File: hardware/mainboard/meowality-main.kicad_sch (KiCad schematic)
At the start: 0 parts

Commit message: Initial 'floorplan' outline
Signed-off-by: gatecat <gatecat@ds0.me>
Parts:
- added H? (x10): MountingHole_Pad, MountingHole:MountingHole_2.7mm_M2.5_Pad_Via, symbol Mechanical:MountingHole_Pad
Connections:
- new net GND: H?.1, H?.1, H?.1, H?.1, H?.1, H?.1, H?.1, H?.1, H?.1, H?.1

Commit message: Placement snapshot
Signed-off-by: gatecat <gatecat@ds0.me>
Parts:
- gave numbers to parts that had none: 10
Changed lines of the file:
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@@
   (symbol (lib_id "power:GND") (at 198.12 97.79 0) (unit 1)
     (in_bom yes) (on_board yes) (fields_autoplaced)
-    (property "Reference" "#PWR?" (id 0) (at 198.12 104.14 0)
+    (property "Reference" "#PWR0300" (id 0) (at 198.12 104.14 0)
       (effects (font (size 1.27 1.27)) hide)
     )
@@
   (symbol (lib_id "Mechanical:MountingHole_Pad") (at 152.4 90.17 0) (unit 1)
     (in_bom yes) (on_board yes) (fields_autoplaced)
-    (property "Reference" "H?" (id 0) (at 154.94 87.6299 0)
+    (property "Reference" "H1" (id 0) (at 154.94 87.6299 0)
       (effects (font (size 1.27 1.27)) (justify left) hide)
     )
@@
   (symbol (lib_id "Mechanical:MountingHole_Pad") (at 193.04 90.17 0) (unit 1)
     (in_bom yes) (on_board yes) (fields_autoplaced)
-    (property "Reference" "H?" (id 0) (at 195.58 87.6299 0)
+    (property "Reference" "H9" (id 0) (at 195.58 87.6299 0)
       (effects (font (size 1.27 1.27)) (justify left) hide)
     )
@@
   (symbol (lib_id "Mechanical:MountingHole_Pad") (at 162.56 90.17 0) (unit 1)
     (in_bom yes) (on_board yes) (fields_autoplaced)
-    (property "Reference" "H?" (id 0) (at 165.1 87.6299 0)
+    (property "Reference" "H3" (id 0) (at 165.1 87.6299 0)
       (effects (font (size 1.27 1.27)) (justify left) hide)
     )
@@
   (symbol (lib_id "Mechanical:MountingHole_Pad") (at 172.72 90.17 0) (unit 1)
     (in_bom yes) (on_board yes) (fields_autoplaced)
-    (property "Reference" "H?" (id 0) (at 175.26 87.6299 0)
+    (property "Reference" "H5" (id 0) (at 175.26 87.6299 0)
       (effects (font (size 1.27 1.27)) (justify left) hide)
     )
@@
   (symbol (lib_id "Mechanical:MountingHole_Pad") (at 157.48 90.17 0) (unit 1)
     (in_bom yes) (on_board yes) (fields_autoplaced)
-    (property "Reference" "H?" (id 0) (at 160.02 87.6299 0)
+    (property "Reference" "H2" (id 0) (at 160.02 87.6299 0)
       (effects (font (size 1.27 1.27)) (justify left) hide)
     )
@@
   (symbol (lib_id "Mechanical:MountingHole_Pad") (at 177.8 90.17 0) (unit 1)
     (in_bom yes) (on_board yes) (fields_autoplaced)
-    (property "Reference" "H?" (id 0) (at 180.34 87.6299 0)
+    (property "Reference" "H6" (id 0) (at 180.34 87.6299 0)
       (effects (font (size 1.27 1.27)) (justify left) hide)
     )
@@
   (symbol (lib_id "Mechanical:MountingHole_Pad") (at 198.12 90.17 0) (unit 1)
     (in_bom yes) (on_board yes) (fields_autoplaced)
-    (property "Reference" "H?" (id 0) (at 200.66 87.6299 0)
+    (property "Reference" "H10" (id 0) (at 200.66 87.6299 0)
       (effects (font (size 1.27 1.27)) (justify left) hide)
     )
@@
   (symbol (lib_id "Mechanical:MountingHole_Pad") (at 187.96 90.17 0) (unit 1)
     (in_bom yes) (on_board yes) (fields_autoplaced)
-    (property "Reference" "H?" (id 0) (at 190.5 87.6299 0)
+    (property "Reference" "H8" (id 0) (at 190.5 87.6299 0)
       (effects (font (size 1.27 1.27)) (justify left) hide)
     )
@@
   (symbol (lib_id "Mechanical:MountingHole_Pad") (at 167.64 90.17 0) (unit 1)
     (in_bom yes) (on_board yes) (fields_autoplaced)
-    (property "Reference" "H?" (id 0) (at 170.18 87.6299 0)
+    (property "Reference" "H4" (id 0) (at 170.18 87.6299 0)
       (effects (font (size 1.27 1.27)) (justify left) hide)
     )
@@
   (symbol (lib_id "Mechanical:MountingHole_Pad") (at 182.88 90.17 0) (unit 1)
     (in_bom yes) (on_board yes) (fields_autoplaced)
-    (property "Reference" "H?" (id 0) (at 185.42 87.6299 0)
+    (property "Reference" "H7" (id 0) (at 185.42 87.6299 0)
       (effects (font (size 1.27 1.27)) (justify left) hide)
     )
@@
       (reference "#PWR0299") (unit 1) (value "+3V3PL") (footprint "")
     )
+    (path "/29964473-8088-4ef2-86ea-4668a18d61fb"
+      (reference "#PWR0300") (unit 1) (value "GND") (footprint "")
+    )
     (path "/1fd619f4-b635-4feb-bd8e-d44522069ea8/6d520754-68d8-4942-8352-d8883ee61a70"
       (reference "#PWR0303") (unit 1) (value "GND") (footprint "")
@@
       (reference "#PWR0367") (unit 1) (value "+3V3PS") (footprint "")
     )
-    (path "/29964473-8088-4ef2-86ea-4668a18d61fb"
-      (reference "#PWR?") (unit 1) (value "GND") (footprint "")
-    )
     (path "/a559f63f-b3a0-4b81-aa6a-605d4da47af6/ec041bff-8a9c-4cb6-b71e-875f2b8c18d1"
       (reference "C1") (unit 1) (value "10µ") (footprint "Capacitor_SMD:C_1206_3216Metric")
@@
     )
     (path "/84ae9301-5488-428b-9d51-06c46b2f0897"
-      (reference "H?") (unit 1) (value "MountingHole_Pad") (footprint "MountingHole:MountingHole_2.7mm_M2.5_Pad_Via")
+      (reference "H1") (unit 1) (value "MountingHole_Pad") (footprint "MountingHole:MountingHole_2.7mm_M2.5_Pad_Via")
+    )
+    (path "/a9b15bc8-d58f-4dce-8008-aeed89e9068b"
+      (reference "H2") (unit 1) (value "MountingHole_Pad") (footprint "MountingHole:MountingHole_2.7mm_M2.5_Pad_Via")
+    )
+    (path "/a070b648-0a85-4170-8a91-599450342e60"
+      (reference "H3") (unit 1) (value "MountingHole_Pad") (footprint "MountingHole:MountingHole_2.7mm_M2.5_Pad_Via")
+    )
+    (path "/e83ea659-2f37-4a3f-a914-2fd0ea472ff3"
+      (reference "H4") (unit 1) (value "MountingHole_Pad") (footprint "MountingHole:MountingHole_2.7mm_M2.5_Pad_Via")
+    )
+    (path "/a34472c6-e5af-4466-bd8c-00051220b9a1"
+      (reference "H5") (unit 1) (value "MountingHole_Pad") (footprint "MountingHole:MountingHole_2.7mm_M2.5_Pad_Via")
+    )
+    (path "/ba6ddcc1-2647-425e-ab4b-d4ffcf66f14b"
+      (reference "H6") (unit 1) (value "MountingHole_Pad") (footprint "MountingHole:MountingHole_2.7mm_M2.5_Pad_Via")
+    )
+    (path "/fc07208b-6f96-45bd-97dc-c33438e49527"
+      (reference "H7") (unit 1) (value "MountingHole_Pad") (footprint "MountingHole:MountingHole_2.7mm_M2.5_Pad_Via")
+    )
+    (path "/e57d0bad-e8df-4b6c-aa3e-bc3f8fd9b788"
+      (reference "H8") (unit 1) (value "MountingHole_Pad") (footprint "MountingHole:MountingHole_2.7mm_M2.5_Pad_Via")
     )
     (path "/9a9fcb89-1441-4dc8-8161-d4c2ca88b33e"
-      (reference "H?") (unit 1) (value "MountingHole_Pad") (footprint "MountingHole:MountingHole_2.7mm_M2.5_Pad_Via")
-    )
-    (path "/a070b648-0a85-4170-8a91-599450342e60"
-      (reference "H?") (unit 1) (value "MountingHole_Pad") (footprint "MountingHole:MountingHole_2.7mm_M2.5_Pad_Via")
-    )
-    (path "/a34472c6-e5af-4466-bd8c-00051220b9a1"
-      (reference "H?") (unit 1) (value "MountingHole_Pad") (footprint "MountingHole:MountingHole_2.7mm_M2.5_Pad_Via")
-    )
-    (path "/a9b15bc8-d58f-4dce-8008-aeed89e9068b"
-      (reference "H?") (unit 1) (value "MountingHole_Pad") (footprint "MountingHole:MountingHole_2.7mm_M2.5_Pad_Via")
-    )
-    (path "/ba6ddcc1-2647-425e-ab4b-d4ffcf66f14b"
-      (reference "H?") (unit 1) (value "MountingHole_Pad") (footprint "MountingHole:MountingHole_2.7mm_M2.5_Pad_Via")
+      (reference "H9") (unit 1) (value "MountingHole_Pad") (footprint "MountingHole:MountingHole_2.7mm_M2.5_Pad_Via")
     )
     (path "/d9faca49-5a69-43b7-ae75-a11a811c721d"
-      (reference "H?") (unit 1) (value "MountingHole_Pad") (footprint "MountingHole:MountingHole_2.7mm_M2.5_Pad_Via")
-    )
-    (path "/e57d0bad-e8df-4b6c-aa3e-bc3f8fd9b788"
-      (reference "H?") (unit 1) (value "MountingHole_Pad") (footprint "MountingHole:MountingHole_2.7mm_M2.5_Pad_Via")
-    )
-    (path "/e83ea659-2f37-4a3f-a914-2fd0ea472ff3"
-      (reference "H?") (unit 1) (value "MountingHole_Pad") (footprint "MountingHole:MountingHole_2.7mm_M2.5_Pad_Via")
-    )
-    (path "/fc07208b-6f96-45bd-97dc-c33438e49527"
-      (reference "H?") (unit 1) (value "MountingHole_Pad") (footprint "MountingHole:MountingHole_2.7mm_M2.5_Pad_Via")
+      (reference "H10") (unit 1) (value "MountingHole_Pad") (footprint "MountingHole:MountingHole_2.7mm_M2.5_Pad_Via")
     )
     (path "/1fd619f4-b635-4feb-bd8e-d44522069ea8/22ac7ace-2c34-4580-9da7-3b6515315310"

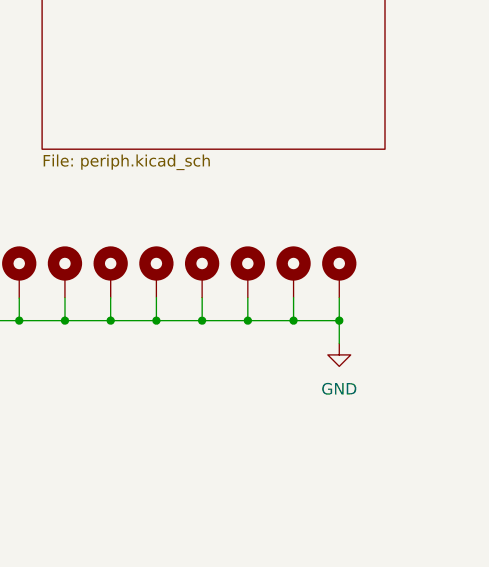
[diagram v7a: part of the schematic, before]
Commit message: Add forgotten M.2 mounting hole
Signed-off-by: gatecat <gatecat@ds0.me>
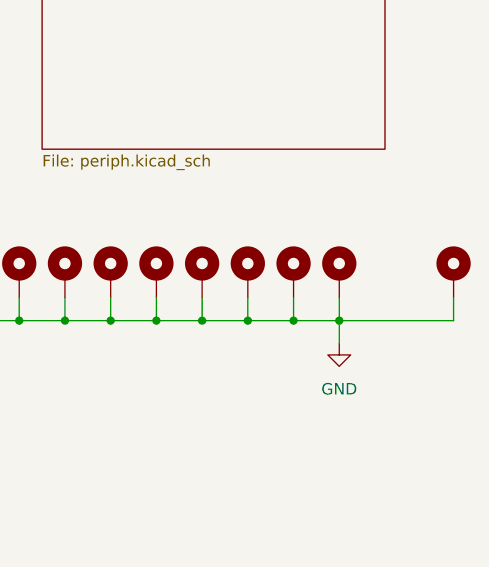
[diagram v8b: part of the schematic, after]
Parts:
- added H11: MountingHole_Pad, meowality:9774025151R, symbol Mechanical:MountingHole_Pad
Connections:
- net GND: now also H11.1
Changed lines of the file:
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@@
+    (stroke (width 0) (type default) (color 0 0 0 0))
+  )
+  (wire (pts (xy 210.82 95.25) (xy 210.82 92.71))
     (stroke (width 0) (type default) (color 0 0 0 0))
   )
@@
   )
   (wire (pts (xy 198.12 95.25) (xy 198.12 97.79))
+    (stroke (width 0) (type default) (color 0 0 0 0))
+  )
+  (wire (pts (xy 198.12 95.25) (xy 210.82 95.25))
     (stroke (width 0) (type default) (color 0 0 0 0))
   )
@@
     )
     (property "Datasheet" "~" (id 3) (at 167.64 90.17 0)
+      (effects (font (size 1.27 1.27)) hide)
+    )
+    (pin "1")
+  )
+  (symbol (lib_id "Mechanical:MountingHole_Pad") (at 210.82 90.17 0) (unit 1)
+    (in_bom yes) (on_board yes) (fields_autoplaced)
+    (property "Reference" "H11" (id 0) (at 213.36 87.6299 0)
+      (effects (font (size 1.27 1.27)) (justify left) hide)
+    )
+    (property "Value" "MountingHole_Pad" (id 1) (at 213.36 88.8999 0)
+      (effects (font (size 1.27 1.27)) (justify left) hide)
+    )
+    (property "Footprint" "meowality:9774025151R" (id 2) (at 210.82 90.17 0)
+      (effects (font (size 1.27 1.27)) hide)
+    )
+    (property "Datasheet" "~" (id 3) (at 210.82 90.17 0)
       (effects (font (size 1.27 1.27)) hide)
     )
@@
       (reference "H10") (unit 1) (value "MountingHole_Pad") (footprint "MountingHole:MountingHole_2.7mm_M2.5_Pad_Via")
     )
+    (path "/ea4601f2-c3d1-49c8-8125-1bced62a50f4"
+      (reference "H11") (unit 1) (value "MountingHole_Pad") (footprint "meowality:9774025151R")
+    )
     (path "/1fd619f4-b635-4feb-bd8e-d44522069ea8/22ac7ace-2c34-4580-9da7-3b6515315310"
